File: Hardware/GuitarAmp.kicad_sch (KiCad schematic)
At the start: 5 parts, among them J1 NMJ4HFD2, U1 TL072

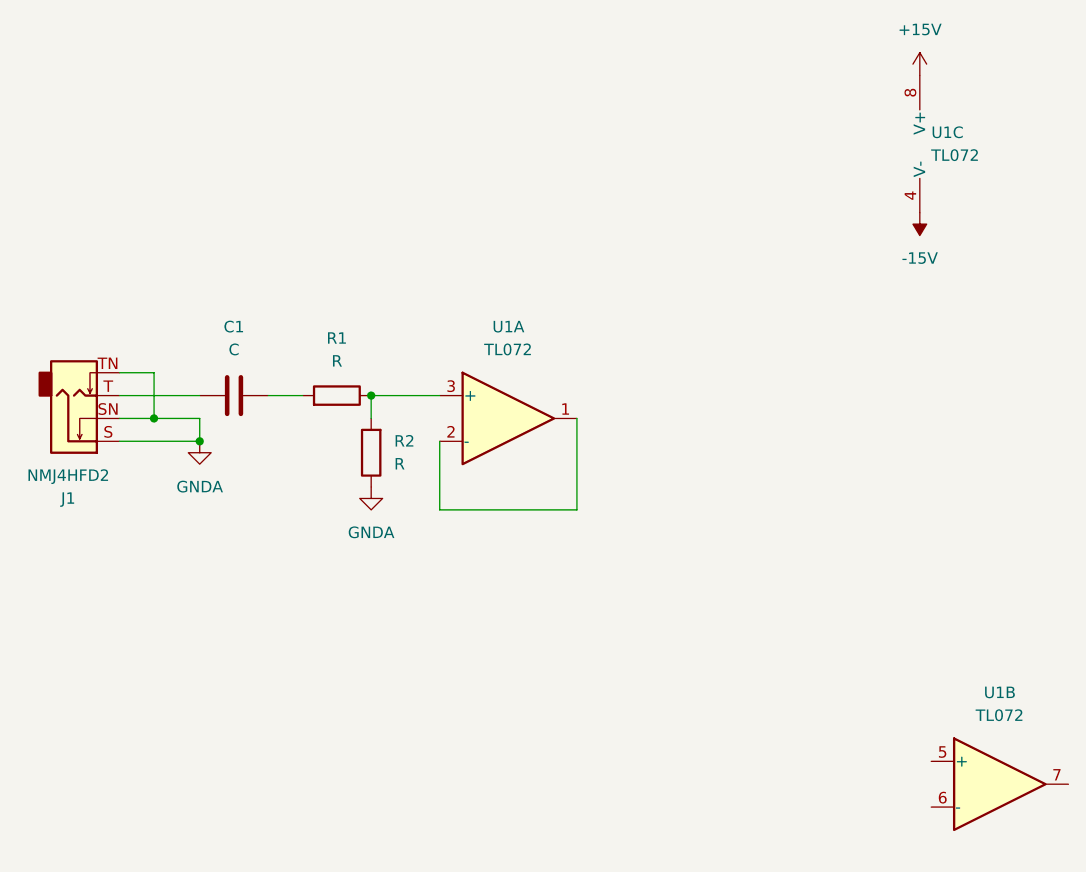
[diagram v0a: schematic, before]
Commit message: Updated schematic with Fender Roc Pro 1000 type input buffer
Signed-off-by: bebenlebricolo <benoittarrade@hotmail.fr>
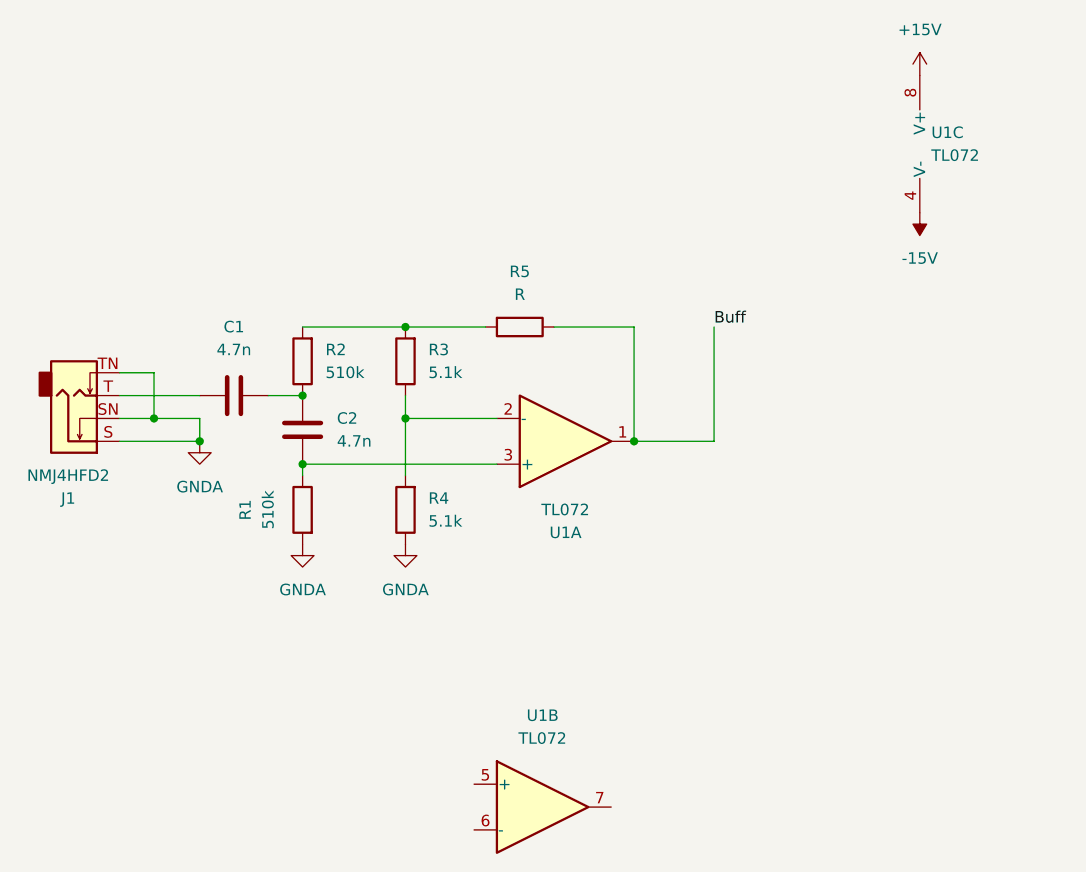
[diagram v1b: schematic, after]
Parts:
- added C2: 4.7n, symbol Device:C
- added R3, R4: 5.1k, symbol Device:R
- added R5: R, symbol Device:R
- C1: value C -> 4.7n
- R1, R2: value R -> 510k
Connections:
- net GNDA: now also R1.2, R4.1; no longer R2.1
- net at C1.2: now also R2.1, C2.2; no longer R1.2
- net at R1.1, U1.3 (+): now also C2.1; no longer R2.2
- net at U1.2 (-): now also R3.1, R4.2; no longer U1.1
- new net: R2.2, R3.2, R5.2
- new net Buff: R5.1, U1.1
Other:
- moved on the sheet: R1, R2, U1A, U1B
